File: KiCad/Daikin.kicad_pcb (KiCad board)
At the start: 2 copper layers, 13.2 x 19.5 mm, 20 parts, among them J1 SPOX, J2 Prog, Q1 PMF170XP,115, Q2 PMF250XNEX, U1 ESP32-PICO-MINI-02, U2 LMR16006+FB

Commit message: Started reverse engineering
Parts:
- added Q3: PMF250XNEX, Package_TO_SOT_SMD:SOT-323_SC-70, B.Cu at (104.2, 48.4)
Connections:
- J1 pad 3: RX -> Net-(J1-Pad3)
- Q1 pad 3: Net-(J1-Pad4) -> Net-(J1-Pad3)
- Q2 pad 3: Net-(J1-Pad4) -> Net-(J1-Pad3)
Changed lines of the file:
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@@
   (net 37 "O")
   (net 38 "Net-(J1-Pad4)")
+  (net 39 "Net-(J1-Pad3)")
   (footprint "RevK:ESP32-PICO-MINI-02" (layer "F.Cu")
     (at 100 44.19325)
@@
       (net 8 "DC") (pinfunction "Pin_2") (pintype "power_out"))
     (pad "3" thru_hole oval (at 1.25 0) (size 1.7 1.85) (drill 0.85) (layers *.Cu *.Mask)
-      (net 3 "RX") (pinfunction "Pin_3") (pintype "passive"))
+      (net 39 "Net-(J1-Pad3)") (pinfunction "Pin_3") (pintype "passive"))
     (pad "4" thru_hole oval (at 3.75 0) (size 1.7 1.85) (drill 0.85) (layers *.Cu *.Mask)
       (net 38 "Net-(J1-Pad4)") (pinfunction "Pin_4") (pintype "passive"))
@@
       (net 11 "EN") (pintype "passive"))
     (model "${KICAD6_3DMODEL_DIR}/Capacitor_SMD.3dshapes/C_0603_1608Metric.step"
+      (offset (xyz 0 0 0))
+      (scale (xyz 1 1 1))
+      (rotate (xyz 0 0 0))
+    )
+  )
+  (footprint "Package_TO_SOT_SMD:SOT-323_SC-70" (layer "B.Cu")
+    (at 104.15 48.35 180)
+    (descr "SOT-323, SC-70")
+    (tags "SOT-323 SC-70")
+    (property "Sheetfile" "Daikin.kicad_sch")
+    (property "Sheetname" "")
+    (attr smd)
+    (fp_text reference "Q3" (at -0.05 1.95) (layer "B.SilkS") hide
+      (effects (font (size 1 1) (thickness 0.15)) (justify mirror))
+    )
+    (fp_text value "PMF250XNEX" (at -0.05 -2.05) (layer "B.Fab")
+      (effects (font (size 1 1) (thickness 0.15)) (justify mirror))
+    )
+    (fp_text user "${REFERENCE}" (at 0 0 90) (layer "B.Fab")
+      (effects (font (size 0.5 0.5) (thickness 0.075)) (justify mirror))
+    )
+    (fp_line (start 0.73 1.16) (end 0.73 0.5) (layer "B.SilkS") (width 0.12))
+    (fp_line (start -0.68 -1.16) (end 0.73 -1.16) (layer "B.SilkS") (width 0.12))
+    (fp_line (start 0.73 -0.5) (end 0.73 -1.16) (layer "B.SilkS") (width 0.12))
+    (fp_line (start 0.73 1.16) (end -1.3 1.16) (layer "B.SilkS") (width 0.12))
+    (fp_line (start -1.7 1.3) (end 1.7 1.3) (layer "B.CrtYd") (width 0.05))
+    (fp_line (start -1.7 -1.3) (end -1.7 1.3) (layer "B.CrtYd") (width 0.05))
+    (fp_line (start 1.7 1.3) (end 1.7 -1.3) (layer "B.CrtYd") (width 0.05))
+    (fp_line (start 1.7 -1.3) (end -1.7 -1.3) (layer "B.CrtYd") (width 0.05))
+    (fp_line (start -0.18 1.1) (end -0.68 0.6) (layer "B.Fab") (width 0.1))
+    (fp_line (start 0.67 1.1) (end -0.18 1.1) (layer "B.Fab") (width 0.1))
+    (fp_line (start 0.67 -1.1) (end -0.68 -1.1) (layer "B.Fab") (width 0.1))
+    (fp_line (start -0.68 0.6) (end -0.68 -1.1) (layer "B.Fab") (width 0.1))
+    (fp_line (start 0.67 1.1) (end 0.67 -1.1) (layer "B.Fab") (width 0.1))
+    (pad "1" smd rect (at -1 0.65 270) (size 0.45 0.7) (layers "B.Cu" "B.Paste" "B.Mask")
+      (net 38 "Net-(J1-Pad4)") (pinfunction "G") (pintype "input"))
+    (pad "2" smd rect (at -1 -0.65 270) (size 0.45 0.7) (layers "B.Cu" "B.Paste" "B.Mask")
+      (net 1 "GND") (pinfunction "S") (pintype "passive"))
+    (pad "3" smd rect (at 1 0 270) (size 0.45 0.7) (layers "B.Cu" "B.Paste" "B.Mask")
+      (net 3 "RX") (pinfunction "D") (pintype "passive"))
+    (model "${KICAD6_3DMODEL_DIR}/Package_TO_SOT_SMD.3dshapes/SOT-323_SC-70.wrl"
       (offset (xyz 0 0 0))
       (scale (xyz 1 1 1))
@@
       (net 3 "RX") (pinfunction "S") (pintype "passive"))
     (pad "3" smd rect (at 1 0 270) (size 0.45 0.7) (layers "B.Cu" "B.Paste" "B.Mask")
-      (net 38 "Net-(J1-Pad4)") (pinfunction "D") (pintype "passive"))
+      (net 39 "Net-(J1-Pad3)") (pinfunction "D") (pintype "passive"))
     (model "${KICAD6_3DMODEL_DIR}/Package_TO_SOT_SMD.3dshapes/SOT-323_SC-70.wrl"
       (offset (xyz 0 0 0))
@@
       (net 1 "GND") (pinfunction "S") (pintype "passive"))
     (pad "3" smd rect (at 1 0 270) (size 0.45 0.7) (layers "B.Cu" "B.Paste" "B.Mask")
-      (net 38 "Net-(J1-Pad4)") (pinfunction "D") (pintype "passive"))
+      (net 39 "Net-(J1-Pad3)") (pinfunction "D") (pintype "passive"))
     (model "${KICAD6_3DMODEL_DIR}/Package_TO_SOT_SMD.3dshapes/SOT-323_SC-70.wrl"
       (offset (xyz 0 0 0))

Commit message: More
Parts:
- J2: moved to B.Cu
- moved J2 10.3 mm to (105.1, 56.8)
- moved Q3 5.65 mm to (104.2, 54.0)
- moved C5 2.48 mm to (96.4, 48.5), turned to 0 degrees
- moved Q1 1.84 mm to (99.9, 54.1)
- moved Q2 1.69 mm to (95.6, 54.0), turned to 0 degrees
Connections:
- Q1 pad 2: RX -> Net-(J1-Pad4)
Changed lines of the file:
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@@
-    )
-  )
-  (footprint "Connector_PinHeader_2.54mm:PinHeader_1x05_P2.54mm_Vertical" (layer "F.Cu")
-    (at 94.75 56.75 90)
-    (descr "Through hole straight pin header, 1x05, 2.54mm pitch, single row")
-    (tags "Through hole pin header THT 1x05 2.54mm single row")
-    (property "Sheetfile" "Daikin.kicad_sch")
-    (property "Sheetname" "")
-    (property "exclude_from_bom" "")
-    (attr through_hole exclude_from_bom)
-    (fp_text reference "J2" (at 0 -2.33 90) (layer "F.SilkS") hide
-      (effects (font (size 1 1) (thickness 0.15)))
-    )
-    (fp_text value "Prog" (at 0 12.49 90) (layer "F.Fab")
-      (effects (font (size 1 1) (thickness 0.15)))
-    )
-    (fp_text user "${REFERENCE}" (at 0 5.08) (layer "F.Fab")
-      (effects (font (size 1 1) (thickness 0.15)))
-    )
-    (fp_line (start -1.33 1.27) (end 1.33 1.27) (layer "F.SilkS") (width 0.12))
-    (fp_line (start -1.33 1.27) (end -1.33 11.49) (layer "F.SilkS") (width 0.12))
-    (fp_line (start -1.33 -1.33) (end 0 -1.33) (layer "F.SilkS") (width 0.12))
-    (fp_line (start -1.33 0) (end -1.33 -1.33) (layer "F.SilkS") (width 0.12))
-    (fp_line (start -1.33 11.49) (end 1.33 11.49) (layer "F.SilkS") (width 0.12))
-    (fp_line (start 1.33 1.27) (end 1.33 11.49) (layer "F.SilkS") (width 0.12))
-    (fp_line (start 1.8 -1.8) (end -1.8 -1.8) (layer "F.CrtYd") (width 0.05))
-    (fp_line (start -1.8 11.95) (end 1.8 11.95) (layer "F.CrtYd") (width 0.05))
-    (fp_line (start 1.8 11.95) (end 1.8 -1.8) (layer "F.CrtYd") (width 0.05))
-    (fp_line (start -1.8 -1.8) (end -1.8 11.95) (layer "F.CrtYd") (width 0.05))
-    (fp_line (start 1.27 -1.27) (end 1.27 11.43) (layer "F.Fab") (width 0.1))
-    (fp_line (start 1.27 11.43) (end -1.27 11.43) (layer "F.Fab") (width 0.1))
-    (fp_line (start -1.27 -0.635) (end -0.635 -1.27) (layer "F.Fab") (width 0.1))
-    (fp_line (start -0.635 -1.27) (end 1.27 -1.27) (layer "F.Fab") (width 0.1))
-    (fp_line (start -1.27 11.43) (end -1.27 -0.635) (layer "F.Fab") (width 0.1))
-    (pad "1" thru_hole rect (at 0 0 90) (size 1.7 1.7) (drill 1) (layers *.Cu *.Mask)
-      (net 1 "GND") (pinfunction "Pin_1") (pintype "power_in"))
-    (pad "2" thru_hole oval (at 0 2.54 90) (size 1.7 1.7) (drill 1) (layers *.Cu *.Mask)
-      (net 25 "GPIO0") (pinfunction "Pin_2") (pintype "passive"))
-    (pad "3" thru_hole oval (at 0 5.08 90) (size 1.7 1.7) (drill 1) (layers *.Cu *.Mask)
-      (net 34 "+3V3") (pinfunction "Pin_3") (pintype "power_in"))
-    (pad "4" thru_hole oval (at 0 7.62 90) (size 1.7 1.7) (drill 1) (layers *.Cu *.Mask)
-      (net 36 "I") (pinfunction "Pin_4") (pintype "passive"))
-    (pad "5" thru_hole oval (at 0 10.16 90) (size 1.7 1.7) (drill 1) (layers *.Cu *.Mask)
-      (net 37 "O") (pinfunction "Pin_5") (pintype "passive"))
-    (model "${KICAD6_3DMODEL_DIR}/Connector_PinHeader_2.54mm.3dshapes/PinHeader_1x05_P2.54mm_Vertical.wrl"
-      (offset (xyz 0 0 0))
-      (scale (xyz 1 1 1))
-      (rotate (xyz 0 0 0))
     )
   )
@@
   )
   (footprint "Package_TO_SOT_SMD:SOT-323_SC-70" (layer "B.Cu")
-    (at 104.15 48.35 180)
+    (at 104.2 54 180)
     (descr "SOT-323, SC-70")
     (tags "SOT-323 SC-70")
@@
     )
   )
+  (footprint "Connector_PinHeader_2.54mm:PinHeader_1x05_P2.54mm_Vertical" (layer "B.Cu")
+    (at 105.1 56.75 90)
+    (descr "Through hole straight pin header, 1x05, 2.54mm pitch, single row")
+    (tags "Through hole pin header THT 1x05 2.54mm single row")
+    (property "Sheetfile" "Daikin.kicad_sch")
+    (property "Sheetname" "")
+    (property "exclude_from_bom" "")
+    (attr through_hole exclude_from_bom)
+    (fp_text reference "J2" (at 0 2.33 270) (layer "B.SilkS") hide
+      (effects (font (size 1 1) (thickness 0.15)) (justify mirror))
+    )
+    (fp_text value "Prog" (at 0 -12.49 270) (layer "B.Fab")
+      (effects (font (size 1 1) (thickness 0.15)) (justify mirror))
+    )
+    (fp_text user "${REFERENCE}" (at 0 -5.08) (layer "B.Fab")
+      (effects (font (size 1 1) (thickness 0.15)) (justify mirror))
+    )
+    (fp_line (start 1.27 1.27) (end 1.27 -11.43) (layer "B.Fab") (width 0.1))
+    (fp_line (start 1.27 -11.43) (end -1.27 -11.43) (layer "B.Fab") (width 0.1))
+    (fp_line (start -1.27 0.635) (end -0.635 1.27) (layer "B.Fab") (width 0.1))
+    (fp_line (start -0.635 1.27) (end 1.27 1.27) (layer "B.Fab") (width 0.1))
+    (fp_line (start -1.27 -11.43) (end -1.27 0.635) (layer "B.Fab") (width 0.1))
+    (pad "1" thru_hole rect (at 0 0 90) (size 1.7 1.7) (drill 1) (layers *.Cu *.Mask)
+      (net 1 "GND") (pinfunction "Pin_1") (pintype "power_in"))
+    (pad "2" thru_hole oval (at 0 -2.54 90) (size 1.7 1.7) (drill 1) (layers *.Cu *.Mask)
+      (net 25 "GPIO0") (pinfunction "Pin_2") (pintype "passive"))
+    (pad "3" thru_hole oval (at 0 -5.08 90) (size 1.7 1.7) (drill 1) (layers *.Cu *.Mask)
+      (net 34 "+3V3") (pinfunction "Pin_3") (pintype "power_in"))
+    (pad "4" thru_hole oval (at 0 -7.62 90) (size 1.7 1.7) (drill 1) (layers *.Cu *.Mask)
+      (net 36 "I") (pinfunction "Pin_4") (pintype "passive"))
+    (pad "5" thru_hole oval (at 0 -10.16 90) (size 1.7 1.7) (drill 1) (layers *.Cu *.Mask)
+      (net 37 "O") (pinfunction "Pin_5") (pintype "passive"))
+    (model "${KICAD6_3DMODEL_DIR}/Connector_PinHeader_2.54mm.3dshapes/PinHeader_1x05_P2.54mm_Vertical.wrl" hide
+      (offset (xyz 0 0 0))
+      (scale (xyz 1 1 1))
+      (rotate (xyz 0 0 0))
+    )
+  )
   (footprint "RevK:Hidden" (layer "B.Cu")
     (at 97.57 44.77)
@@
   )
   (footprint "Package_TO_SOT_SMD:SOT-323_SC-70" (layer "B.Cu")
-    (at 101.735714 54 180)
+    (at 99.9 54.1 180)
     (descr "SOT-323, SC-70")
     (tags "SOT-323 SC-70")
@@
       (net 2 "TX") (pinfunction "G") (pintype "input"))
     (pad "2" smd rect (at -1 -0.65 270) (size 0.45 0.7) (layers "B.Cu" "B.Paste" "B.Mask")
-      (net 3 "RX") (pinfunction "S") (pintype "passive"))
+      (net 38 "Net-(J1-Pad4)") (pinfunction "S") (pintype "passive"))
     (pad "3" smd rect (at 1 0 270) (size 0.45 0.7) (layers "B.Cu" "B.Paste" "B.Mask")
       (net 39 "Net-(J1-Pad3)") (pinfunction "D") (pintype "passive"))
@@
   )
   (footprint "Package_TO_SOT_SMD:SOT-323_SC-70" (layer "B.Cu")
-    (at 97.285714 54 180)
+    (at 95.6 54)
     (descr "SOT-323, SC-70")
     (tags "SOT-323 SC-70")
@@
     (fp_line (start 0.67 1.1) (end -0.18 1.1) (layer "B.Fab") (width 0.1))
     (fp_line (start -0.68 0.6) (end -0.68 -1.1) (layer "B.Fab") (width 0.1))
-    (pad "1" smd rect (at -1 0.65 270) (size 0.45 0.7) (layers "B.Cu" "B.Paste" "B.Mask")
+    (pad "1" smd rect (at -1 0.65 90) (size 0.45 0.7) (layers "B.Cu" "B.Paste" "B.Mask")
       (net 2 "TX") (pinfunction "G") (pintype "input"))
-    (pad "2" smd rect (at -1 -0.65 270) (size 0.45 0.7) (layers "B.Cu" "B.Paste" "B.Mask")
+    (pad "2" smd rect (at -1 -0.65 90) (size 0.45 0.7) (layers "B.Cu" "B.Paste" "B.Mask")
       (net 1 "GND") (pinfunction "S") (pintype "passive"))
-    (pad "3" smd rect (at 1 0 270) (size 0.45 0.7) (layers "B.Cu" "B.Paste" "B.Mask")
+    (pad "3" smd rect (at 1 0 90) (size 0.45 0.7) (layers "B.Cu" "B.Paste" "B.Mask")
       (net 39 "Net-(J1-Pad3)") (pinfunction "D") (pintype "passive"))
     (model "${KICAD6_3DMODEL_DIR}/Package_TO_SOT_SMD.3dshapes/SOT-323_SC-70.wrl"
@@
   )
   (footprint "RevK:C_0603" (layer "B.Cu")
-    (at 94.7 50.3 -90)
+    (at 96.4 48.5)
     (descr "Capacitor SMD 0603 (1608 Metric), square (rectangular) end terminal, IPC_7351 nominal, (Body size source: IPC-SM-782 page 76, https://www.pcb-3d.com/wordpress/wp-content/uploads/ipc-sm-782a_amendment_1_and_2.pdf), generated with kicad-footprint-generator")
     (tags "capacitor")
@@
     (property "Sheetname" "")
     (attr smd)
-    (fp_text reference "C5" (at -1.6 0) (layer "B.SilkS") hide
-      (effects (font (size 0.5 0.5) (thickness 0.08)) (justify mirror))
-    )
-    (fp_text value "100nF" (at 0 0 90) (layer "B.Fab")
+    (fp_text reference "C5" (at -1.6 0 90) (layer "B.SilkS") hide
+      (effects (font (size 0.5 0.5) (thickness 0.08)) (justify mirror))
+    )
+    (fp_text value "100nF" (at 0 0) (layer "B.Fab")
       (effects (font (size 0.4 0.4) (thickness 0.08)) (justify mirror))
     )
-    (fp_text user "${REFERENCE}" (at 0 0.8 90) (layer "B.Fab")
+    (fp_text user "${REFERENCE}" (at 0 0.8) (layer "B.Fab")
       (effects (font (size 0.4 0.4) (thickness 0.06)) (justify mirror))
     )
@@
     (fp_line (start -0.8 -0.4) (end -0.8 0.4) (layer "B.Fab") (width 0.1))
     (fp_line (start 0.8 0.4) (end 0.8 -0.4) (layer "B.Fab") (width 0.1))
-    (pad "1" smd roundrect (at -0.775 0 270) (size 0.8 0.95) (layers "B.Cu" "B.Paste" "B.Mask") (roundrect_rratio 0.25)
+    (pad "1" smd roundrect (at -0.775 0) (size 0.8 0.95) (layers "B.Cu" "B.Paste" "B.Mask") (roundrect_rratio 0.25)
       (net 34 "+3V3") (pintype "passive"))
-    (pad "2" smd roundrect (at 0.775 0 270) (size 0.8 0.95) (layers "B.Cu" "B.Paste" "B.Mask") (roundrect_rratio 0.25)
+    (pad "2" smd roundrect (at 0.775 0) (size 0.8 0.95) (layers "B.Cu" "B.Paste" "B.Mask") (roundrect_rratio 0.25)
       (net 1 "GND") (pintype "passive"))
     (model "${KICAD6_3DMODEL_DIR}/Capacitor_SMD.3dshapes/C_0603_1608Metric.step"
@@
     (effects (font (size 0.5 0.5) (thickness 0.08)) (justify mirror))
   )
-  (gr_text "www.me.uk" (at 100.5 49) (layer "B.SilkS")
+  (gr_text "www.me.uk" (at 100.3 49.7) (layer "B.SilkS")
     (effects (font (size 1 1) (thickness 0.15)) (justify mirror))
   )

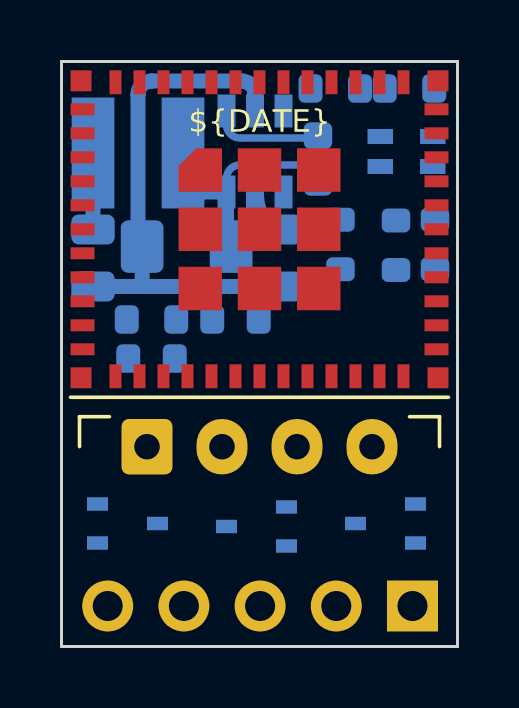
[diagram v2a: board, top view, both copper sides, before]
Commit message: Tx will have to be 3.3V, which seems to work OK.
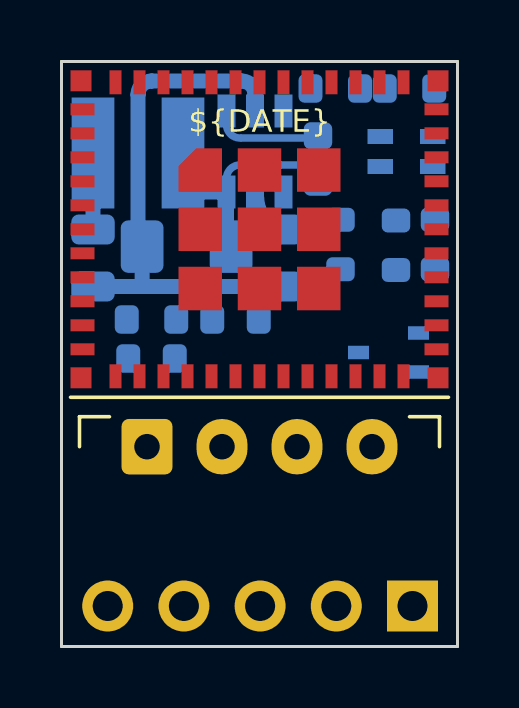
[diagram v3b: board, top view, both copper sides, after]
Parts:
- removed Q1: PMF170XP,115, Package_TO_SOT_SMD:SOT-323_SC-70
- removed Q2: PMF250XNEX, Package_TO_SOT_SMD:SOT-323_SC-70
- moved Q3 5.70 mm to (104.3, 48.3)
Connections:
- J1 pad 3: Net-(J1-Pad3) -> TX
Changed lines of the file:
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@@
   (net 37 "O")
   (net 38 "Net-(J1-Pad4)")
-  (net 39 "Net-(J1-Pad3)")
   (footprint "RevK:ESP32-PICO-MINI-02" (layer "F.Cu")
     (at 100 44.19325)
@@
       (net 8 "DC") (pinfunction "Pin_2") (pintype "power_out"))
     (pad "3" thru_hole oval (at 1.25 0) (size 1.7 1.85) (drill 0.85) (layers *.Cu *.Mask)
-      (net 39 "Net-(J1-Pad3)") (pinfunction "Pin_3") (pintype "passive"))
+      (net 2 "TX") (pinfunction "Pin_3") (pintype "passive"))
     (pad "4" thru_hole oval (at 3.75 0) (size 1.7 1.85) (drill 0.85) (layers *.Cu *.Mask)
       (net 38 "Net-(J1-Pad4)") (pinfunction "Pin_4") (pintype "passive"))
@@
   )
   (footprint "Package_TO_SOT_SMD:SOT-323_SC-70" (layer "B.Cu")
-    (at 104.2 54 180)
+    (at 104.3 48.3 180)
     (descr "SOT-323, SC-70")
     (tags "SOT-323 SC-70")
@@
     (fp_circle (center 0 0) (end 0.2 0) (layer "Cmts.User") (width 0.12) (fill none))
   )
-  (footprint "Package_TO_SOT_SMD:SOT-323_SC-70" (layer "B.Cu")
-    (at 99.9 54.1 180)
-    (descr "SOT-323, SC-70")
-    (tags "SOT-323 SC-70")
-    (property "Note" "Any P-Channel SOT323 that does 3.3V/0.5A")
-    (property "Sheetfile" "Daikin.kicad_sch")
-    (property "Sheetname" "")
-    (attr smd)
-    (fp_text reference "Q1" (at -0.05 1.95) (layer "B.SilkS") hide
-      (effects (font (size 1 1) (thickness 0.15)) (justify mirror))
-    )
-    (fp_text value "PMF170XP,115" (at -0.05 -2.05) (layer "B.Fab")
-      (effects (font (size 1 1) (thickness 0.15)) (justify mirror))
-    )
-    (fp_text user "${REFERENCE}" (at 0 0 90) (layer "B.Fab")
-      (effects (font (size 0.5 0.5) (thickness 0.075)) (justify mirror))
-    )
-    (fp_line (start -0.68 -1.16) (end 0.73 -1.16) (layer "B.SilkS") (width 0.12))
-    (fp_line (start 0.73 1.16) (end 0.73 0.5) (layer "B.SilkS") (width 0.12))
-    (fp_line (start 0.73 1.16) (end -1.3 1.16) (layer "B.SilkS") (width 0.12))
-    (fp_line (start 0.73 -0.5) (end 0.73 -1.16) (layer "B.SilkS") (width 0.12))
-    (fp_line (start -1.7 -1.3) (end -1.7 1.3) (layer "B.CrtYd") (width 0.05))
-    (fp_line (start 1.7 1.3) (end 1.7 -1.3) (layer "B.CrtYd") (width 0.05))
-    (fp_line (start -1.7 1.3) (end 1.7 1.3) (layer "B.CrtYd") (width 0.05))
-    (fp_line (start 1.7 -1.3) (end -1.7 -1.3) (layer "B.CrtYd") (width 0.05))
-    (fp_line (start -0.68 0.6) (end -0.68 -1.1) (layer "B.Fab") (width 0.1))
-    (fp_line (start 0.67 -1.1) (end -0.68 -1.1) (layer "B.Fab") (width 0.1))
-    (fp_line (start -0.18 1.1) (end -0.68 0.6) (layer "B.Fab") (width 0.1))
-    (fp_line (start 0.67 1.1) (end -0.18 1.1) (layer "B.Fab") (width 0.1))
-    (fp_line (start 0.67 1.1) (end 0.67 -1.1) (layer "B.Fab") (width 0.1))
-    (pad "1" smd rect (at -1 0.65 270) (size 0.45 0.7) (layers "B.Cu" "B.Paste" "B.Mask")
-      (net 2 "TX") (pinfunction "G") (pintype "input"))
-    (pad "2" smd rect (at -1 -0.65 270) (size 0.45 0.7) (layers "B.Cu" "B.Paste" "B.Mask")
-      (net 38 "Net-(J1-Pad4)") (pinfunction "S") (pintype "passive"))
-    (pad "3" smd rect (at 1 0 270) (size 0.45 0.7) (layers "B.Cu" "B.Paste" "B.Mask")
-      (net 39 "Net-(J1-Pad3)") (pinfunction "D") (pintype "passive"))
-    (model "${KICAD6_3DMODEL_DIR}/Package_TO_SOT_SMD.3dshapes/SOT-323_SC-70.wrl"
-      (offset (xyz 0 0 0))
-      (scale (xyz 1 1 1))
-      (rotate (xyz 0 0 0))
-    )
-  )
   (footprint "RevK:Hidden" (layer "B.Cu")
     (at 101.95 41.85 -90)
@@
     (fp_circle (center 0 0) (end 0.2 0) (layer "Cmts.User") (width 0.12) (fill none))
   )
-  (footprint "Package_TO_SOT_SMD:SOT-323_SC-70" (layer "B.Cu")
-    (at 95.6 54)
-    (descr "SOT-323, SC-70")
-    (tags "SOT-323 SC-70")
-    (property "Sheetfile" "Daikin.kicad_sch")
-    (property "Sheetname" "")
-    (attr smd)
-    (fp_text reference "Q2" (at -0.05 1.95) (layer "B.SilkS") hide
-      (effects (font (size 1 1) (thickness 0.15)) (justify mirror))
-    )
-    (fp_text value "PMF250XNEX" (at -0.05 -2.05) (layer "B.Fab")
-      (effects (font (size 1 1) (thickness 0.15)) (justify mirror))
-    )
-    (fp_text user "${REFERENCE}" (at 0 0 90) (layer "B.Fab")
-      (effects (font (size 0.5 0.5) (thickness 0.075)) (justify mirror))
-    )
-    (fp_line (start 0.73 1.16) (end -1.3 1.16) (layer "B.SilkS") (width 0.12))
-    (fp_line (start -0.68 -1.16) (end 0.73 -1.16) (layer "B.SilkS") (width 0.12))
-    (fp_line (start 0.73 -0.5) (end 0.73 -1.16) (layer "B.SilkS") (width 0.12))
-    (fp_line (start 0.73 1.16) (end 0.73 0.5) (layer "B.SilkS") (width 0.12))
-    (fp_line (start -1.7 -1.3) (end -1.7 1.3) (layer "B.CrtYd") (width 0.05))
-    (fp_line (start 1.7 -1.3) (end -1.7 -1.3) (layer "B.CrtYd") (width 0.05))
-    (fp_line (start 1.7 1.3) (end 1.7 -1.3) (layer "B.CrtYd") (width 0.05))
-    (fp_line (start -1.7 1.3) (end 1.7 1.3) (layer "B.CrtYd") (width 0.05))
-    (fp_line (start 0.67 -1.1) (end -0.68 -1.1) (layer "B.Fab") (width 0.1))
-    (fp_line (start 0.67 1.1) (end 0.67 -1.1) (layer "B.Fab") (width 0.1))
-    (fp_line (start -0.18 1.1) (end -0.68 0.6) (layer "B.Fab") (width 0.1))
-    (fp_line (start 0.67 1.1) (end -0.18 1.1) (layer "B.Fab") (width 0.1))
-    (fp_line (start -0.68 0.6) (end -0.68 -1.1) (layer "B.Fab") (width 0.1))
-    (pad "1" smd rect (at -1 0.65 90) (size 0.45 0.7) (layers "B.Cu" "B.Paste" "B.Mask")
-      (net 2 "TX") (pinfunction "G") (pintype "input"))
-    (pad "2" smd rect (at -1 -0.65 90) (size 0.45 0.7) (layers "B.Cu" "B.Paste" "B.Mask")
-      (net 1 "GND") (pinfunction "S") (pintype "passive"))
-    (pad "3" smd rect (at 1 0 90) (size 0.45 0.7) (layers "B.Cu" "B.Paste" "B.Mask")
-      (net 39 "Net-(J1-Pad3)") (pinfunction "D") (pintype "passive"))
-    (model "${KICAD6_3DMODEL_DIR}/Package_TO_SOT_SMD.3dshapes/SOT-323_SC-70.wrl"
-      (offset (xyz 0 0 0))
-      (scale (xyz 1 1 1))
-      (rotate (xyz 0 0 0))
-    )
-  )
   (footprint "RevK:LED-RGB-1.6x1.6" (layer "B.Cu")

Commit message: PCb design
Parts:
- moved Q3 0.81 mm to (103.5, 48.2)
- moved D1 0.60 mm to (104.9, 42.2)
- moved R1 0.60 mm to (103.3, 44.7)
- moved J2 0.35 mm to (105.1, 56.4)
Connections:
- U1 pad 28: unconnected-(U1-Pad28) -> G
- U1 pad 33: G -> R
- U1 pad 34: R -> unconnected-(U1-Pad34)
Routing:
- net GND: track 0.00 -> 73.5 mm, vias 0 -> 5
- net +3V3: track 0.00 -> 33.9 mm, vias 0 -> 4
- net O: track 0.00 -> 21.6 mm, vias 0 -> 1
- net I: track 0.00 -> 17.7 mm, vias 0 -> 1
- net DC: track 0.00 -> 10.3 mm
- net GPIO0: track 0.00 -> 8.29 mm
- net R: track 0.00 -> 8.24 mm, vias 0 -> 1
- net Net-(J1-Pad4): track 0.00 -> 6.68 mm
- net EN: track 0.00 -> 6.58 mm, vias 0 -> 1
- net TX: track 0.00 -> 4.61 mm
- net RX: track 0.00 -> 3.87 mm, vias 0 -> 1
- net Net-(R5-Pad2): track 0.00 -> 3.65 mm
- net Net-(D1-Pad2): track 0.00 -> 2.66 mm
- net G: track 0.00 -> 2.50 mm, vias 0 -> 1
- net B: track 0.00 -> 2.23 mm, vias 0 -> 1
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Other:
- board text added: "${DATE}"
- board text added: "0"
- board text added: "19/8/7"
- board text added: "26"
- board text added: "27"
- board text added: "3.3V"
- board text added: "DC"
- board text added: "GND"
- board text added: "Rx"
- board text added: "Tx"
- board text removed: "RGB: 22/19/7"
